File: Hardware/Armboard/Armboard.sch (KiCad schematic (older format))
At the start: 18 parts

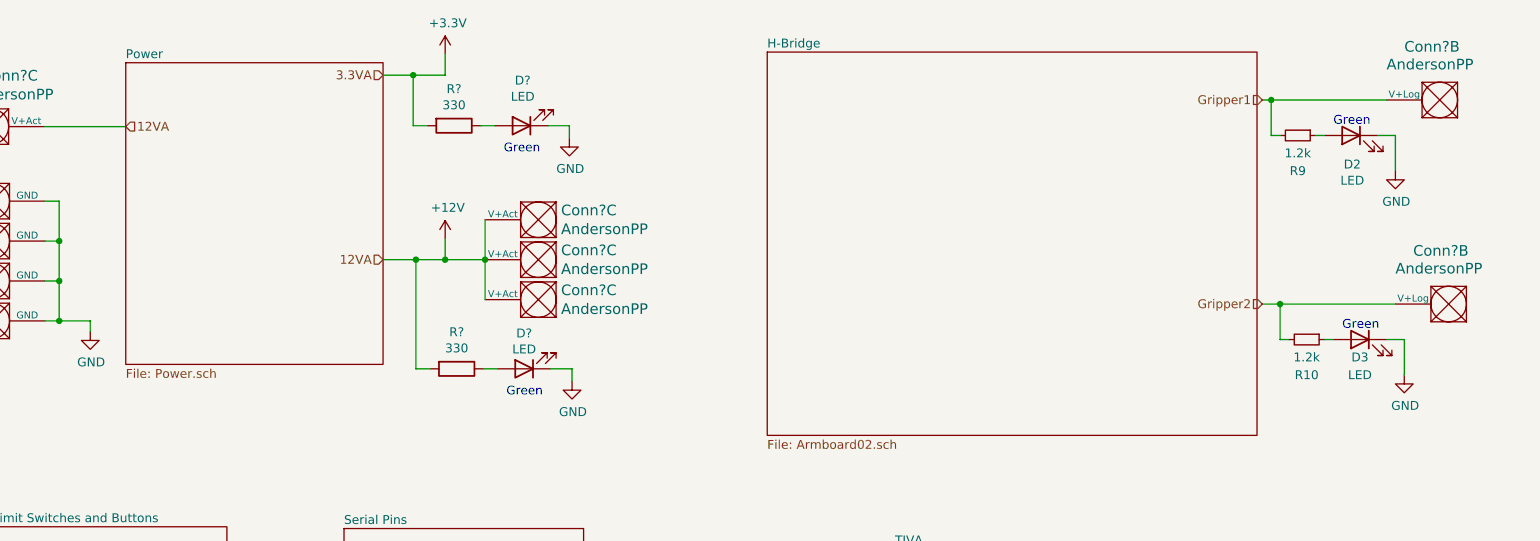
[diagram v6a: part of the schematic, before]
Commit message: Review 2 board changes
-Connected the busses on the power and H-Bridge
-Changed the resistor value to 1.2k
-Fixed some of the pin locations on the TIVA
-Added ferrites to the H-Bridge
-Connected the buses so that they all highlight correctly
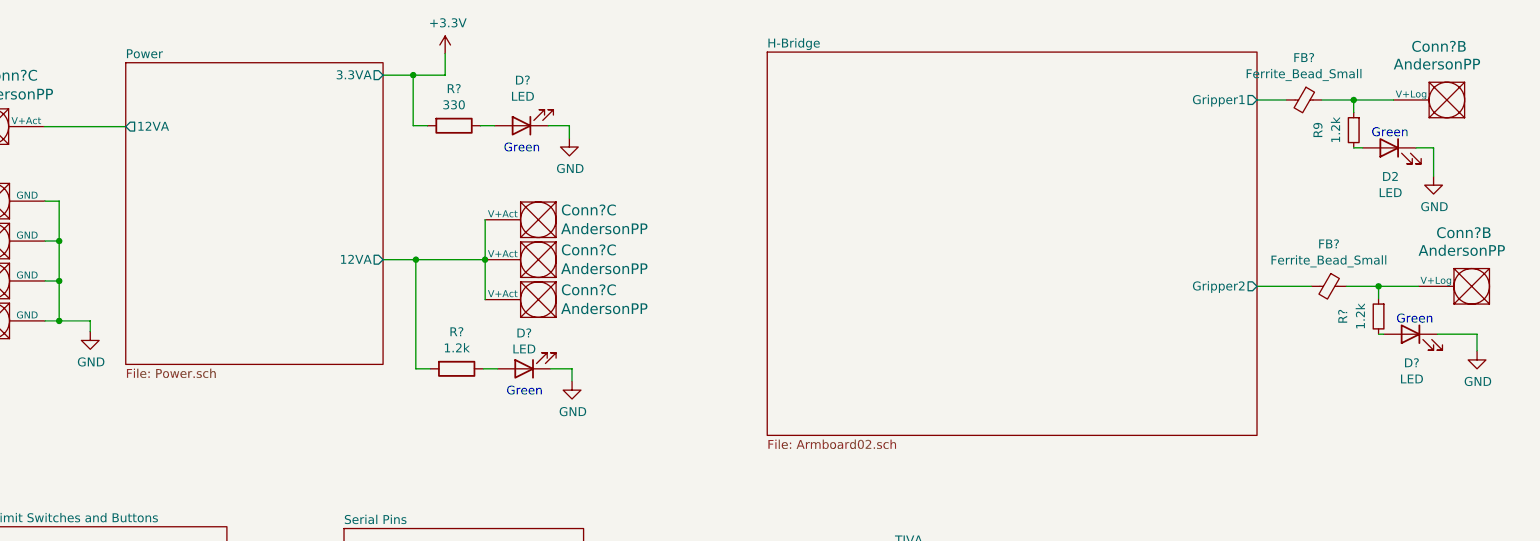
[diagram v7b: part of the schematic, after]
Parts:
- removed Conn?: AndersonPP, symbol MRDT_Connectors:AndersonPP
- removed D3: LED, symbol Device:LED
- removed R10: 1.2k, symbol Device:R_Small
- added Conn?: AndersonPP, symbol MRDT_Connectors:AndersonPP
- added D?: LED, symbol Device:LED
- added FB? (x2): Ferrite_Bead_Small, symbol Device:Ferrite_Bead_Small
- added R?: 1.2k, symbol Device:R_Small
- R?: value 330 -> 1.2k
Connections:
- net GND: now also D?.1 (K)
- net at R9.1: now also Conn?.2 (V+Log), FB?.1; no longer D2.2 (A)
- net +12V renamed Power/12VA
- net Power/12VA: no longer Conn?.3 (V+Act)
- net Gripper1: no longer names the net of R9.2
- net Gripper1: now also D2.2 (A); no longer Conn?.2 (V+Log)
- new net: Conn?.2 (V+Log), FB?.1, R?.1
- new net: D?.2 (A), R?.2
- new net H-Bridge/Gripper1: FB?.2
- new net H-Bridge/Gripper2: FB?.2
- new net Power/12VA: Conn?.3 (V+Act)
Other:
- moved on the sheet: Conn?B, D2, R9
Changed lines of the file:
@@
 F0 "Power" 50
 F1 "Power.sch" 50
+F2 "3.3VA" O R 3945 1110 50
+F3 "12VA" O R 3945 2150 50
+F4 "12VA" O L 2495 1400 50
 $EndSheet
 $Comp
@@
 	1    0    0    -1
 $EndComp
-Text HLabel 2495 1400 2    50   Input ~ 0
-12VA
-Text HLabel 3945 1110 0    50   Input ~ 0
-3.3VA
 $Comp
 L power:+3.3V #PWR?
@@
 $EndComp
 $Sheet
-S 6110 980  2760 2160
-U 5F7381FC
-F0 "H-Bridge" 50
-F1 "Armboard02.sch" 50
-$EndSheet
-$Sheet
 S 6830 3780 2750 2100
 U 5F7383E1
@@
 Text Notes 6530 7160 0    138  ~ 28
 Armboard Rev1
-Text HLabel 8900 1250 0    50   Input ~ 0
-Gripper1
-Wire Wire Line
-	8900 1250 8950 1250
-Wire Wire Line
-	8950 1450 9000 1450
 $Comp
 L Device:R_Small R9
 U 1 1 5F8623A9
-P 9100 1450
-F 0 "R9" V 9300 1450 50  0000 C CNN
-F 1 "1.2k" V 9200 1450 50  0000 C CNN
-F 2 "" H 9100 1450 50  0001 C CNN
-F 3 "~" H 9100 1450 50  0001 C CNN
-	1    9100 1450
-	0    1    1    0
+P 9415 1420
+F 0 "R9" V 9615 1420 50  0000 C CNN
+F 1 "1.2k" V 9515 1420 50  0000 C CNN
+F 2 "" H 9415 1420 50  0001 C CNN
+F 3 "~" H 9415 1420 50  0001 C CNN
+	1    9415 1420
+	-1   0    0    -1
 $EndComp
 $Comp
 L Device:LED D2
 U 1 1 5F862E5D
-P 9400 1450
-F 0 "D2" H 9393 1287 50  0000 C CNN
-F 1 "LED" H 9393 1196 50  0000 C CNN
-F 2 "" H 9400 1450 50  0001 C CNN
-F 3 "~" H 9400 1450 50  0001 C CNN
-	1    9400 1450
-	-1   0    0    -1
-$EndComp
-Wire Wire Line
-	9250 1450 9200 1450
-Wire Wire Line
-	9550 1450 9650 1450
+P 9615 1520
+F 0 "D2" H 9608 1357 50  0000 C CNN
+F 1 "LED" H 9608 1266 50  0000 C CNN
+F 2 "" H 9615 1520 50  0001 C CNN
+F 3 "~" H 9615 1520 50  0001 C CNN
+	1    9615 1520
+	-1   0    0    -1
+$EndComp
+Wire Wire Line
+	9465 1520 9415 1520
+Wire Wire Line
+	9765 1520 9865 1520
 $Comp
 L power:GND #PWR?
 U 1 1 5F863B11
-P 9650 1650
-F 0 "#PWR?" H 9650 1400 50  0001 C CNN
-F 1 "GND" H 9655 1477 50  0000 C CNN
-F 2 "" H 9650 1650 50  0001 C CNN
-F 3 "" H 9650 1650 50  0001 C CNN
-	1    9650 1650
+P 9865 1680
+F 0 "#PWR?" H 9865 1430 50  0001 C CNN
+F 1 "GND" H 9870 1507 50  0000 C CNN
+F 2 "" H 9865 1680 50  0001 C CNN
+F 3 "" H 9865 1680 50  0001 C CNN
+	1    9865 1680
 	1    0    0    -1
 $EndComp
@@
 L MRDT_Connectors:AndersonPP Conn?
 U 2 1 5F864024
-P 10000 1350
-F 0 "Conn?" H 10300 1750 60  0000 R CNN
-F 1 "AndersonPP" H 10400 1650 60  0000 R CNN
-F 2 "" H 9850 800 60  0001 C CNN
-F 3 "" H 9850 800 60  0001 C CNN
-	2    10000 1350
-	-1   0    0    -1
-$EndComp
-Wire Wire Line
-	8950 1250 8950 1450
-Wire Wire Line
-	8950 1250 9600 1250
-Connection ~ 8950 1250
-Wire Wire Line
-	9650 1450 9650 1650
-Wire Wire Line
-	9000 2600 9050 2600
-$Comp
-L Device:R_Small R10
-U 1 1 5F8695AA
-P 9150 2600
-F 0 "R10" V 9350 2600 50  0000 C CNN
-F 1 "1.2k" V 9250 2600 50  0000 C CNN
-F 2 "" H 9150 2600 50  0001 C CNN
-F 3 "~" H 9150 2600 50  0001 C CNN
-	1    9150 2600
-	0    1    1    0
-$EndComp
-$Comp
-L Device:LED D3
-U 1 1 5F8695B0
-P 9450 2600
-F 0 "D3" H 9450 2500 50  0000 C CNN
-F 1 "LED" H 9450 2400 50  0000 C CNN
-F 2 "" H 9450 2600 50  0001 C CNN
-F 3 "~" H 9450 2600 50  0001 C CNN
-	1    9450 2600
-	-1   0    0    -1
-$EndComp
-Wire Wire Line
-	9300 2600 9250 2600
-Wire Wire Line
-	9600 2600 9700 2600
-$Comp
-L power:GND #PWR?
-U 1 1 5F8695B8
-P 9700 2800
-F 0 "#PWR?" H 9700 2550 50  0001 C CNN
-F 1 "GND" H 9705 2627 50  0000 C CNN
-F 2 "" H 9700 2800 50  0001 C CNN
-F 3 "" H 9700 2800 50  0001 C CNN
-	1    9700 2800
-	1    0    0    -1
-$EndComp
-$Comp
-L MRDT_Connectors:AndersonPP Conn?
-U 2 1 5F8695BE
-P 10050 2500
-F 0 "Conn?" H 10350 2900 60  0000 R CNN
-F 1 "AndersonPP" H 10450 2800 60  0000 R CNN
-F 2 "" H 9900 1950 60  0001 C CNN
-F 3 "" H 9900 1950 60  0001 C CNN
-	2    10050 2500
-	-1   0    0    -1
-$EndComp
-Wire Wire Line
-	9000 2400 9000 2600
-Wire Wire Line
-	9000 2400 9650 2400
-Connection ~ 9000 2400
-Wire Wire Line
-	9700 2600 9700 2800
-Text HLabel 8900 2400 0    50   Input ~ 0
-Gripper2
-Wire Wire Line
-	8900 2400 9000 2400
-Text Notes 9300 1400 0    50   ~ 0
+P 10040 1350
+F 0 "Conn?" H 10340 1750 60  0000 R CNN
+F 1 "AndersonPP" H 10440 1650 60  0000 R CNN
+F 2 "" H 9890 800 60  0001 C CNN
+F 3 "" H 9890 800 60  0001 C CNN
+	2    10040 1350
+	-1   0    0    -1
+$EndComp
+Text Notes 9515 1470 0    50   ~ 0
 Green
-Text Notes 9350 2550 0    50   ~ 0
-Green
-Text HLabel 3945 2150 0    50   Input ~ 0
-12VA
 $Comp
 L Device:R R?
@@
 AR Path="/5F870C74" Ref="R?"  Part="1"
 F 0 "R?" V 4153 2765 50  0000 C CNN
-F 1 "330" V 4244 2765 50  0000 C CNN
+F 1 "1.2k" V 4244 2765 50  0000 C CNN
 F 2 "" V 4290 2765 50  0001 C CNN
 F 3 "~" H 4360 2765 50  0001 C CNN
@@
 	5010 2765 5010 2835
 Wire Wire Line
-	4295 2150 4295 2030
-Wire Wire Line
 	4210 2765 4130 2765
-$Comp
-L power:+12V #PWR?
-U 1 1 5F8721E3
-P 4295 2030
-F 0 "#PWR?" H 4295 1880 50  0001 C CNN
-F 1 "+12V" H 4310 2203 50  0000 C CNN
-F 2 "" H 4295 2030 50  0001 C CNN
-F 3 "" H 4295 2030 50  0001 C CNN
-	1    4295 2030
-	1    0    0    -1
-$EndComp
 $Comp
 L MRDT_Connectors:AndersonPP Conn?
@@
 Wire Wire Line
 	3945 2150 4130 2150
-Wire Wire Line
-	4295 2150 4520 2150
-Connection ~ 4295 2150
 Connection ~ 4520 2150
 Wire Wire Line
@@
 	4520 2150 4520 2375
 Connection ~ 4130 2150
-Wire Wire Line
-	4130 2150 4295 2150
 Wire Wire Line
 	4130 2150 4130 2765
@@
 Wire Wire Line
 	2120 2045 2120 2270
+$Comp
+L Device:Ferrite_Bead_Small FB?
+U 1 1 5F96BE6D
+P 9135 1250
+F 0 "FB?" V 8898 1250 50  0000 C CNN
+F 1 "Ferrite_Bead_Small" V 8989 1250 50  0000 C CNN
+F 2 "" V 9065 1250 50  0001 C CNN
+F 3 "~" H 9135 1250 50  0001 C CNN
+	1    9135 1250
+	0    1    1    0
+$EndComp
+Wire Wire Line
+	4130 2150 4520 2150
+Wire Wire Line
+	8870 1250 9035 1250
+Wire Wire Line
+	9235 1250 9415 1250
+Wire Wire Line
+	9865 1520 9865 1680
+Wire Wire Line
+	9415 1320 9415 1250
+Connection ~ 9415 1250
+Wire Wire Line
+	9415 1250 9640 1250
+$Comp
+L Device:LED D?
+U 1 1 5F98CE15
+P 9735 2570
+F 0 "D?" H 9728 2407 50  0000 C CNN
+F 1 "LED" H 9728 2316 50  0000 C CNN
+F 2 "" H 9735 2570 50  0001 C CNN
+F 3 "~" H 9735 2570 50  0001 C CNN
+	1    9735 2570
+	-1   0    0    -1
+$EndComp
+$Comp
+L power:GND #PWR?
+U 1 1 5F98CE21
+P 10110 2665
+F 0 "#PWR?" H 10110 2415 50  0001 C CNN
+F 1 "GND" H 10115 2492 50  0000 C CNN
+F 2 "" H 10110 2665 50  0001 C CNN
+F 3 "" H 10110 2665 50  0001 C CNN
+	1    10110 2665
+	1    0    0    -1
+$EndComp
+$Comp
+L MRDT_Connectors:AndersonPP Conn?
+U 2 1 5F98CE2B
+P 10180 2400
+F 0 "Conn?" H 10480 2800 60  0000 R CNN
+F 1 "AndersonPP" H 10580 2700 60  0000 R CNN
+F 2 "" H 10030 1850 60  0001 C CNN
+F 3 "" H 10030 1850 60  0001 C CNN
+	2    10180 2400
+	-1   0    0    -1
+$EndComp
+Text Notes 9655 2520 0    50   ~ 0
+Green
+Wire Wire Line
+	9555 2300 9780 2300
+Connection ~ 9555 2300
+Wire Wire Line
+	9555 2370 9555 2300
+Wire Wire Line
+	9375 2300 9555 2300
+$Comp
+L Device:Ferrite_Bead_Small FB?
+U 1 1 5F98CE36
+P 9275 2300
+F 0 "FB?" V 9038 2300 50  0000 C CNN
+F 1 "Ferrite_Bead_Small" V 9129 2300 50  0000 C CNN
+F 2 "" V 9205 2300 50  0001 C CNN
+F 3 "~" H 9275 2300 50  0001 C CNN
+	1    9275 2300
+	0    1    1    0
+$EndComp
+$Comp
+L Device:R_Small R?
+U 1 1 5F98CE0B
+P 9555 2470
+F 0 "R?" V 9755 2470 50  0000 C CNN
+F 1 "1.2k" V 9655 2470 50  0000 C CNN
+F 2 "" H 9555 2470 50  0001 C CNN
+F 3 "~" H 9555 2470 50  0001 C CNN
+	1    9555 2470
+	-1   0    0    -1
+$EndComp
+Wire Wire Line
+	9555 2570 9585 2570
+Wire Wire Line
+	10110 2570 10110 2665
+Wire Wire Line
+	9885 2570 10110 2570
+$Sheet
+S 6110 980  2760 2160
+U 5F7381FC
+F0 "H-Bridge" 50
+F1 "Armboard02.sch" 50
+F2 "Gripper1" O R 8870 1250 50
+F3 "Gripper2" O R 8870 2300 50
+$EndSheet
+Wire Wire Line
+	8870 2300 9175 2300
 $EndSCHEMATC

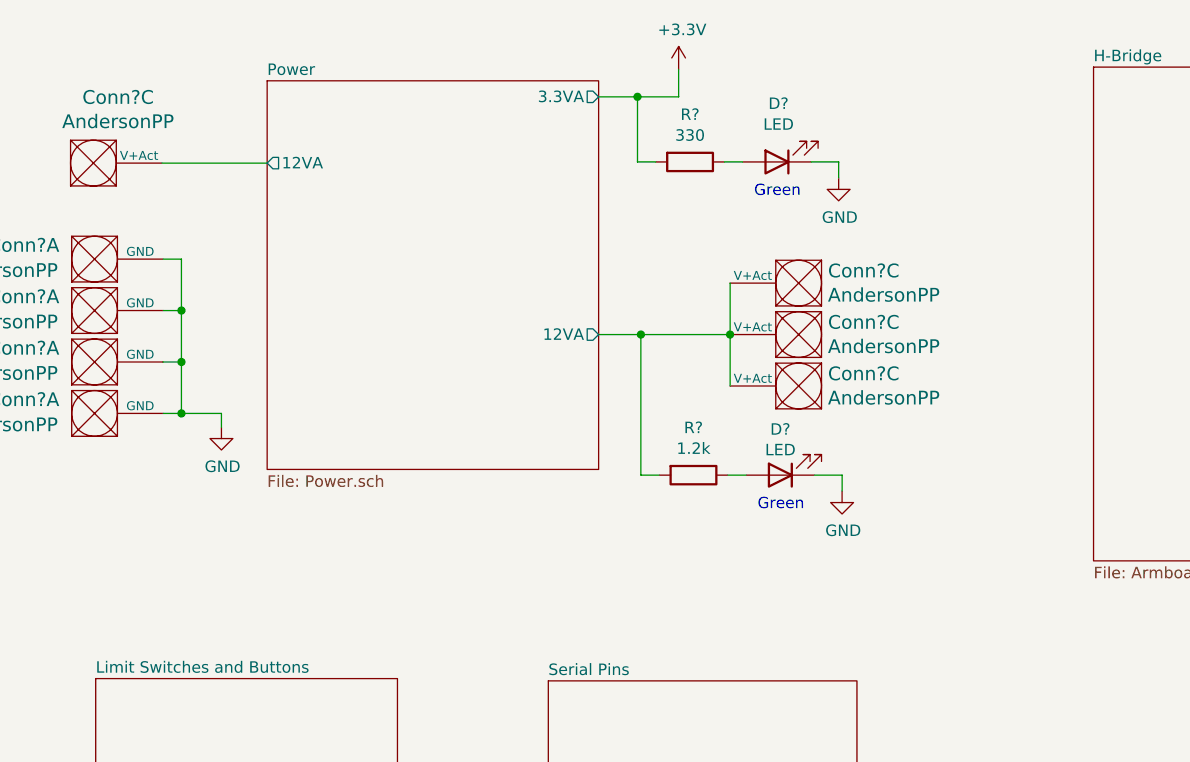
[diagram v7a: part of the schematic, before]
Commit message: Fixed changes from review 2 of circuit board
except the LED indicators
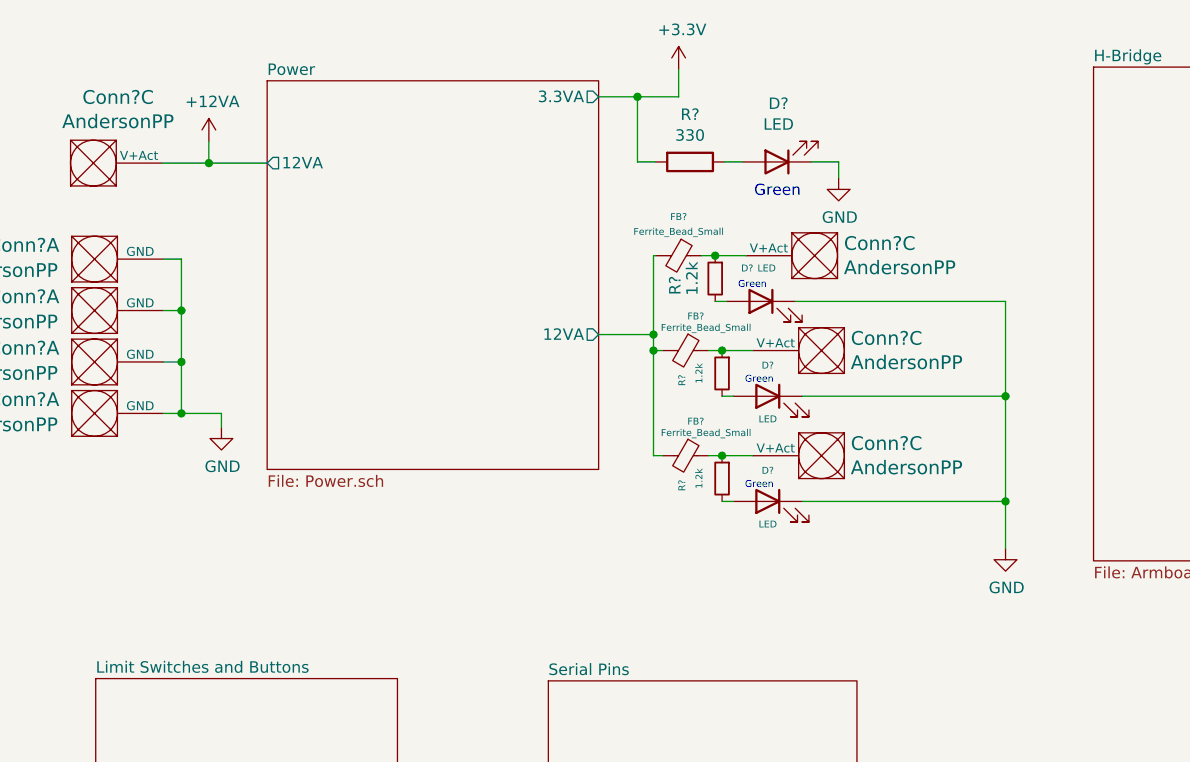
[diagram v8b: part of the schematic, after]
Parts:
- removed Conn? (x2): AndersonPP, symbol MRDT_Connectors:AndersonPP
- removed D?: LED, symbol Device:LED
- removed R?: 1.2k, symbol Device:R
- added Conn? (x2): AndersonPP, symbol MRDT_Connectors:AndersonPP
- added D? (x3): LED, symbol Device:LED
- added FB? (x3): Ferrite_Bead_Small, symbol Device:Ferrite_Bead_Small
- added R? (x3): 1.2k, symbol Device:R_Small
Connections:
- net GND: now also D?.1 (K), D?.1 (K), D?.1 (K)
- net Power/12VA: now also FB?.2, FB?.2, FB?.2; no longer Conn?.3 (V+Act)
- net Power/12VA: no longer names the net of Conn?.3 (V+Act)
- net Power/12VA: now also FB?.1, R?.1
- new net: D?.2 (A), R?.2 (x3)
- new net: Conn?.3 (V+Act), FB?.1, R?.1 (x2)
- new net +12VA: Conn?.3 (V+Act)
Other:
- moved on the sheet: Conn?C
